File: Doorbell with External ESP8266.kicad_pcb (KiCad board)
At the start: 4 copper layers, 70 x 50 mm, 31 parts, among them J101 Transformer, J102 From Rectifier, J103 To Rectifier, J104 Chime, J105 Button, K101 Relay, Q101 Q_NMOS_GSD, U101 WeMos_D1_mini, U102 XC6220B331MR-G, U103 EL817

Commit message: Added JLCPCB silkscreen object for order #
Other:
- board text added: "JLCJLCJLCJLC"
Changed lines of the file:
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@@
 		(layer "Edge.Cuts")
+	)
+	(gr_text "JLCJLCJLCJLC"
+		(at 44 22.4 0)
+		(layer "B.SilkS")
+		(effects
+			(font
+				(size 1 1)
+				(thickness 0.153)
+			)
+			(justify left bottom mirror)
+		)
 	)
 	(gr_text "Rly"

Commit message: Moved power to different level & made JLCPCB order
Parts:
- removed C101: 22uF, Capacitor_SMD:C_0603_1608Metric
- removed C102: 4.7uF, Capacitor_SMD:C_0603_1608Metric
- removed U102: XC6220B331MR-G, Package_TO_SOT_SMD:SOT-23-5
- moved F101 3.70 mm to (39.9, 41.0), turned to 0 degrees
- moved REF** 0.55 mm to (34.6, 24.9)
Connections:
- U101 pad 8: unconnected-(U101-3V3-Pad8) -> +3V3
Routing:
- net +3V3: track 49.9 -> 20.8 mm, vias 2 -> 4
- net VCC: track 69.8 -> 53.9 mm
- net GND: track 16.6 -> 10.1 mm, vias 9 -> 6
- net Net-(J102-Pin_2): track 23.2 -> 26.7 mm
- net /RELAY_LED: track 31.6 -> 29.5 mm
- net /CHIME: track 9.24 -> 10.1 mm
- added copper zone on In2.Cu, net +3V3

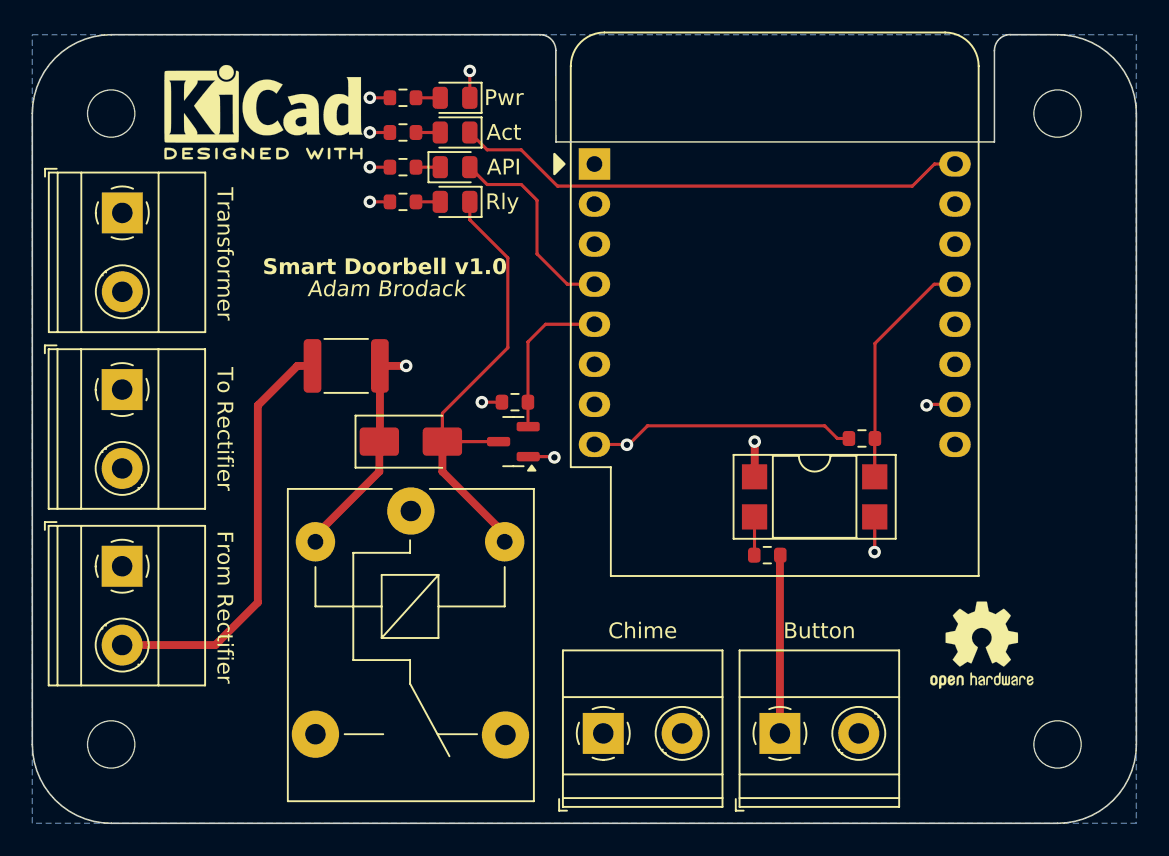
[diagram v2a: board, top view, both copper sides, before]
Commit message: Fixed MOSFET for relay & moved some parts around to make it better
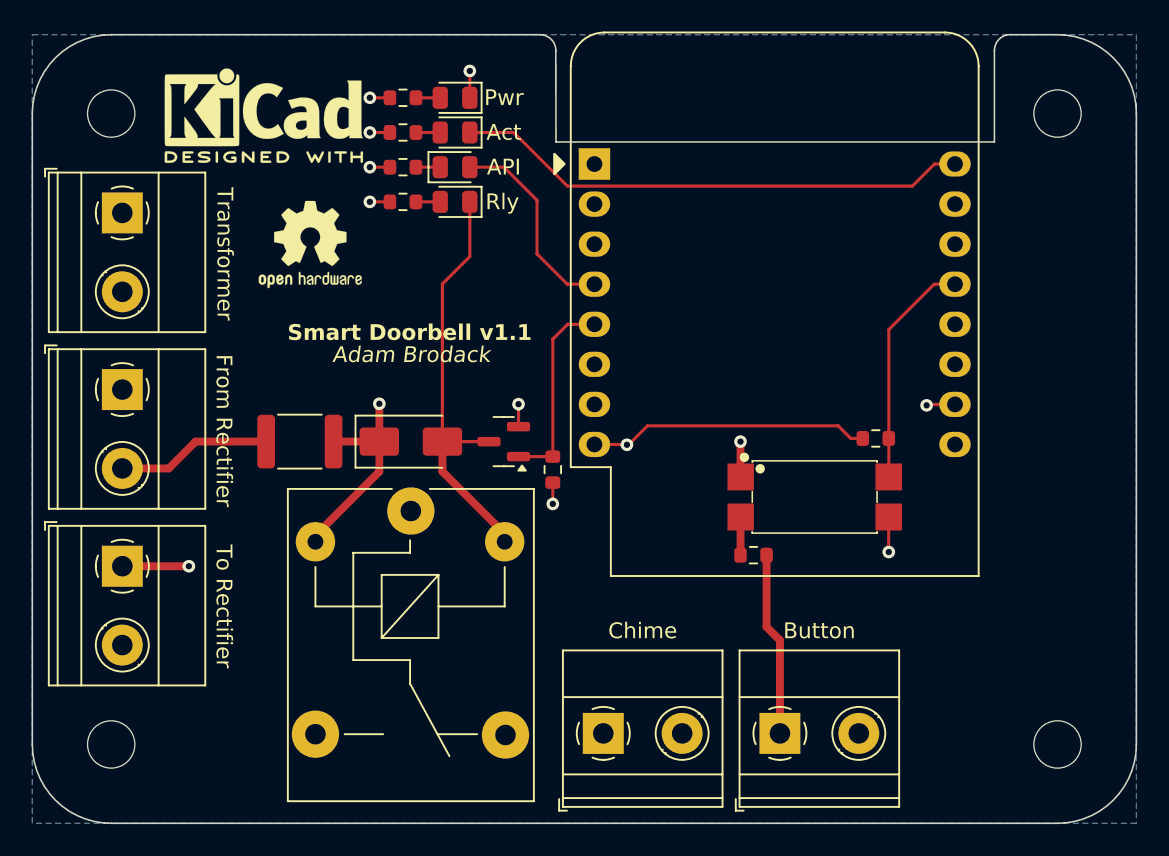
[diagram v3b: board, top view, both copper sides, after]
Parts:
- U103: footprint Package_DIP:DIP-4_W7.62mm_SMDSocket_SmallPads -> footprints:EL817S1(C)(TU)-F
- moved REF** 49.6 mm to (37.6, 33.3)
- moved J102 11.2 mm to (25.7, 42.5)
- moved J103 11.2 mm to (25.7, 53.7)
- moved F101 5.63 mm to (37.0, 45.8)
- moved R105 4.90 mm to (53.0, 47.6), turned to -90 degrees
- moved R106 0.88 mm to (65.7, 53.0)
- moved R107 0.88 mm to (73.5, 45.6)
- moved Q101 0.61 mm to (49.9, 45.8)
- moved REF** 0.23 mm to (34.7, 25.1)
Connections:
- Q101 pad 1: GND -> /CHIME
- Q101 pad 2: /CHIME -> GND
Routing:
- net Net-(J102-Pin_2): track 26.7 -> 9.82 mm
- net /AC_B: track 59.4 -> 70.1 mm
- net /RELAY_LED: track 29.5 -> 26.9 mm
- net /CHIME: track 10.1 -> 12.7 mm
- net /AC_A: track 44.2 -> 45.9 mm, vias 0 -> 1
- net +3V3: track 20.8 -> 21.7 mm
